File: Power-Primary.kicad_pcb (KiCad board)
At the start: 2 copper layers, 226.1 x 72.4 mm, 77 parts, among them J1 HV in, J10 SPARE, J11 SPARE, J12 SPARE, J13 SPARE, J14 SPARE, J15 SPARE, J16 SPARE, J17 SPARE, J2 Dashboard, J3 Telemetry, J4 Motor, J5 MPPT 1, J6 MPPT 2, J7 BPS, J8 Primary Disconn., J9 SPARE, U1 Mean_Well_12V

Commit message: completed Hannah's edits
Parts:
- removed the G*** at (226.1, 104.1)
- added REF**: MountingHole_3mm, MountingHole:MountingHole_3.7mm, F.Cu at (175.3, 113.0)
- moved REF** 1.60 mm to (237.5, 124.2)
- moved REF** 1.27 mm to (237.5, 60.2)
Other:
- board size 226.1 x 72.4 mm -> 225.8 x 71.9 mm

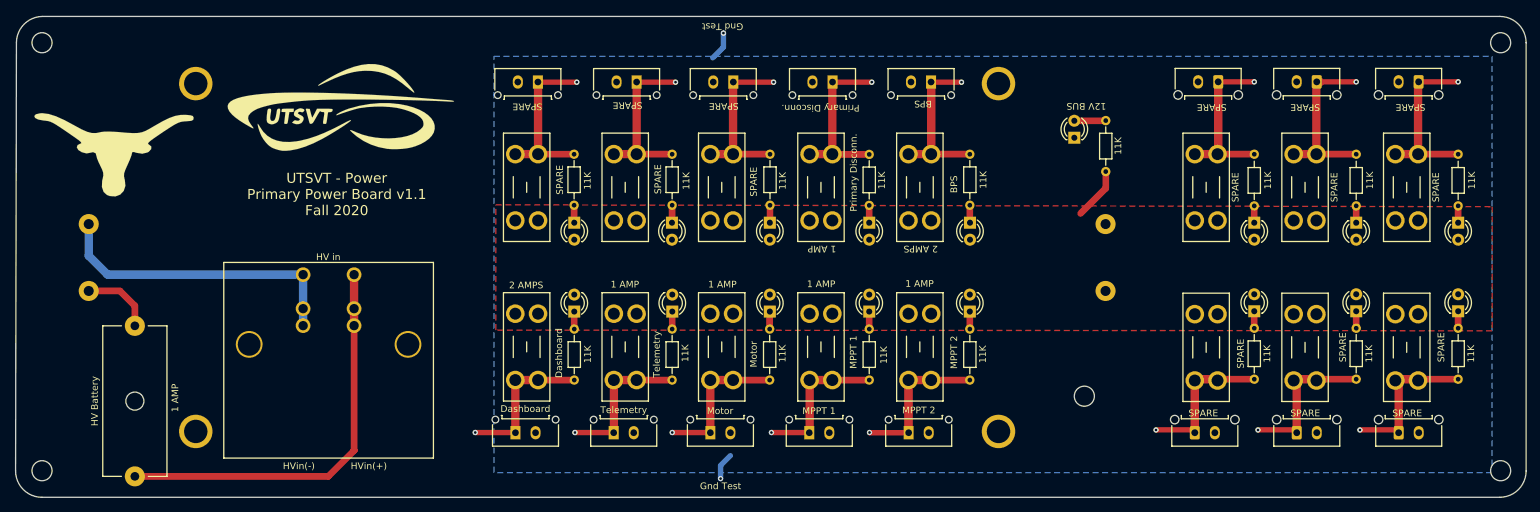
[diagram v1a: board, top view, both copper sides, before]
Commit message: Sijin's edits, mounting hole and power planes
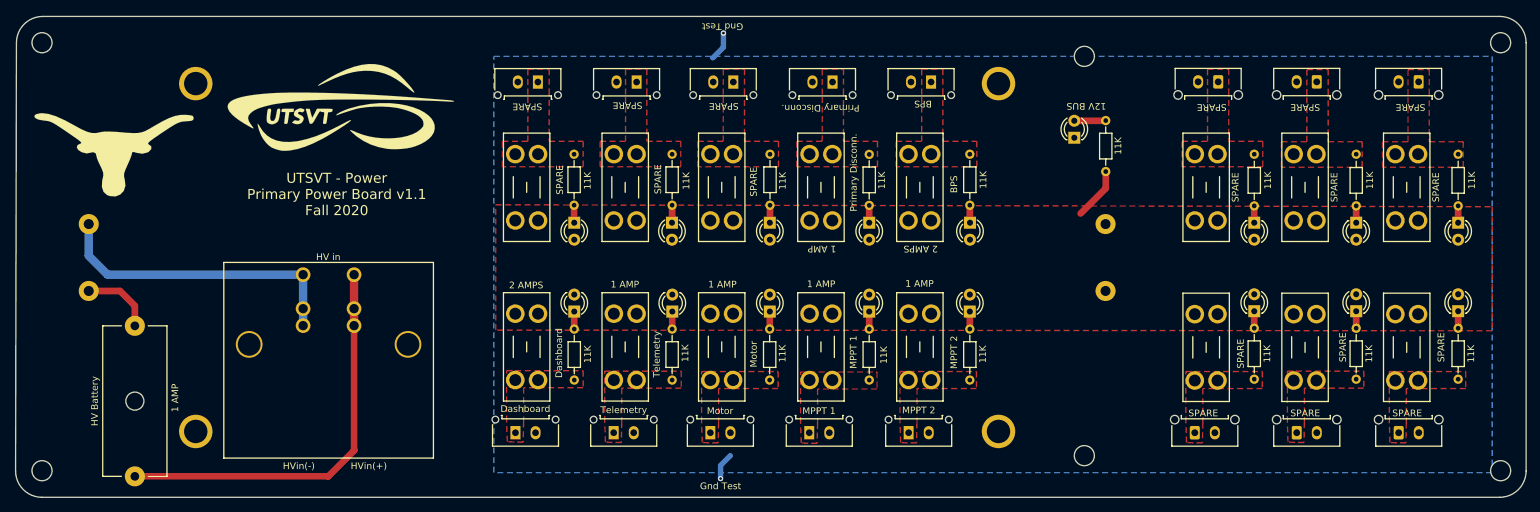
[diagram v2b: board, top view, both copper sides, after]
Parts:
- added REF**: MountingHole_3mm, MountingHole:MountingHole_3.7mm, F.Cu at (175.3, 62.2)
- moved REF** 8.89 mm to (175.3, 121.9)
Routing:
- net Net-(F15-Pad2): track 26.3 -> 0.34 mm, vias 1 -> 0
- net Net-(F9-Pad2): track 25.8 -> 0.14 mm, vias 1 -> 0
- net Net-(F16-Pad2): track 25.9 -> 0.23 mm, vias 1 -> 0
- net Net-(F8-Pad2): track 25.7 -> 0.21 mm, vias 1 -> 0
- net Net-(F11-Pad2): track 25.4 -> 0.12 mm, vias 1 -> 0
- net Net-(F10-Pad2): track 25.3 -> 0.07 mm, vias 1 -> 0
- net Net-(F17-Pad2): track 25.3 -> 0.30 mm, vias 1 -> 0
- net Net-(F7-Pad2): track 24.6 -> 0.12 mm, vias 1 -> 0
- net Net-(F6-Pad2): track 23.0 -> 0.12 mm, vias 1 -> 0
- net Net-(F2-Pad2): track 22.7 -> 0.08 mm, vias 1 -> 0
- net Net-(F4-Pad2): track 22.5 -> 0.04 mm, vias 1 -> 0
- net Net-(F5-Pad2): track 22.7 -> 0.30 mm, vias 1 -> 0
- net Net-(F3-Pad2): track 22.4 -> 0.12 mm, vias 1 -> 0
- net Net-(F13-Pad2): track 22.3 -> 0.00 mm, vias 1 -> 0
- net Net-(F14-Pad2): track 22.3 -> 0.00 mm, vias 1 -> 0
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- added copper zone on F.Cu, net Net-(F10-Pad2)
- added copper zone on F.Cu, net Net-(F11-Pad2)
- added copper zone on F.Cu, net Net-(F12-Pad2)
- added copper zone on F.Cu, net Net-(F13-Pad2)
- added copper zone on F.Cu, net Net-(F14-Pad2)
- added copper zone on F.Cu, net Net-(F15-Pad2)
- added copper zone on F.Cu, net Net-(F16-Pad2)
- added copper zone on F.Cu, net Net-(F17-Pad2)
- added copper zone on F.Cu, net Net-(F2-Pad2)
- added copper zone on F.Cu, net Net-(F3-Pad2)
- added copper zone on F.Cu, net Net-(F4-Pad2)
- added copper zone on F.Cu, net Net-(F5-Pad2)
- added copper zone on F.Cu, net Net-(F6-Pad2)
- added copper zone on F.Cu, net Net-(F7-Pad2)
- added copper zone on F.Cu, net Net-(F8-Pad2)
- added copper zone on F.Cu, net Net-(F9-Pad2)

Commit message: Deletes gerbers from this because added to release and adds dimensions
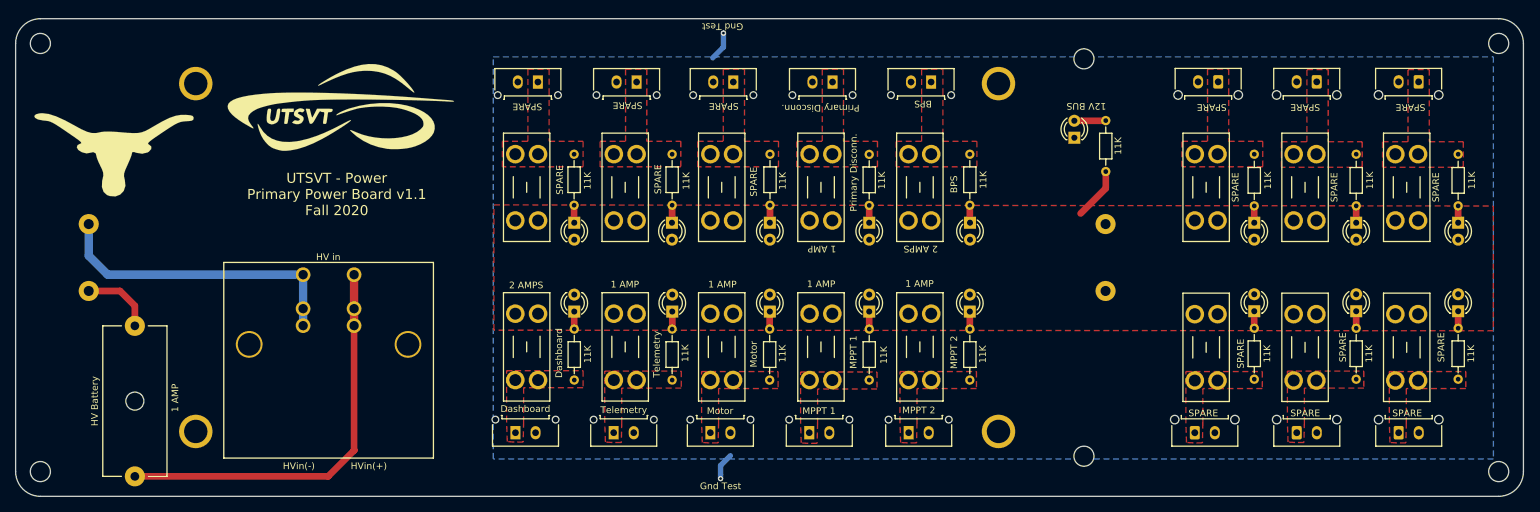
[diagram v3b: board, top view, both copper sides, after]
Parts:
- removed the REF** at (175.3, 121.9)
- removed the REF** at (237.5, 60.2)
- added REF**: MountingHole_3mm, MountingHole:MountingHole_3.7mm, F.Cu at (175.2, 122.0)
- added REF**: MountingHole_3mm, MountingHole:MountingHole_3.7mm, F.Cu at (237.2, 60.3)
- moved REF** 0.37 mm to (175.2, 62.6)
- moved REF** 0.32 mm to (237.2, 124.3)
- moved REF** 0.28 mm to (19.2, 124.3)
- moved REF** 0.27 mm to (19.2, 60.3)
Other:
- board size 225.8 x 71.9 mm -> 225.4 x 71.4 mm
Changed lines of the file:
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@@
-(kicad_pcb (version 20171130) (host pcbnew "(5.1.6)-1")
+(kicad_pcb (version 20171130) (host pcbnew "(5.1.5)-3")
   (general
     (thickness 1.6)
-    (drawings 27)
+    (drawings 29)
     (tracks 95)
     (zones 0)
@@
     (44 Edge.Cuts user)
     (45 Margin user)
-    (46 B.CrtYd user)
-    (47 F.CrtYd user)
-    (48 B.Fab user)
-    (49 F.Fab user)
+    (46 B.CrtYd user hide)
+    (47 F.CrtYd user hide)
+    (48 B.Fab user hide)
+    (49 F.Fab user hide)
   )
   (setup
-    (last_trace_width 0.25)
+    (last_trace_width 0.8)
     (user_trace_width 0.8)
     (user_trace_width 1)
@@
       (drillshape 0)
       (scaleselection 1)
-      (outputdirectory ""))
+      (outputdirectory "Gerbers/"))
   )
   (net 0 "")
@@
   )
   (module MountingHole:MountingHole_3.7mm (layer F.Cu)
-    (at 175.26 62.23)
+    (at 175.2 62.6)
     (descr "Mounting Hole 3.7mm, no annular")
     (tags "mounting hole 3.7mm no annular")
@@
   )
   (module MountingHole:MountingHole_3.7mm (layer F.Cu)
-    (at 175.26 121.92)
+    (at 175.2 122)
     (descr "Mounting Hole 3.7mm, no annular")
     (tags "mounting hole 3.7mm no annular")
@@
   )
   (module MountingHole:MountingHole_3.7mm (layer F.Cu)
-    (at 19.44624 60.19292)
+    (at 19.2 60.3)
     (descr "Mounting Hole 3.7mm, no annular")
     (tags "mounting hole 3.7mm no annular")
@@
   )
   (module MountingHole:MountingHole_3.7mm (layer F.Cu)
-    (at 237.49 60.19292)
+    (at 237.2 60.3)
     (descr "Mounting Hole 3.7mm, no annular")
     (tags "mounting hole 3.7mm no annular")
@@
   )
   (module MountingHole:MountingHole_3.7mm (layer F.Cu)
-    (at 237.49 124.17044)
+    (at 237.2 124.3)
     (descr "Mounting Hole 3.7mm, no annular")
     (tags "mounting hole 3.7mm no annular")
@@
   )
   (module MountingHole:MountingHole_3.7mm (layer F.Cu)
-    (at 19.44624 124.17044)
+    (at 19.2 124.3)
     (descr "Mounting Hole 3.7mm, no annular")
     (tags "mounting hole 3.7mm no annular")
@@
     )
   )
-  (gr_arc (start 237.363 124.206) (end 237.363 128.143) (angle -90) (layer Edge.Cuts) (width 0.15))
-  (gr_arc (start 19.558 60.198) (end 19.558 56.261) (angle -90) (layer Edge.Cuts) (width 0.15))
-  (gr_arc (start 19.431 124.206) (end 15.494 124.206) (angle -90) (layer Edge.Cuts) (width 0.15))
-  (gr_arc (start 237.363 60.198) (end 241.3 60.198) (angle -90) (layer Edge.Cuts) (width 0.15))
+  (dimension 225.4 (width 0.15) (layer Cmts.User)
+    (gr_text "225.400 mm" (at 128.2 52.2) (layer Cmts.User)
+      (effects (font (size 1 1) (thickness 0.15)))
+    )
+    (feature1 (pts (xy 15.5 60.3) (xy 15.5 52.913579)))
+    (feature2 (pts (xy 240.9 60.3) (xy 240.9 52.913579)))
+    (crossbar (pts (xy 240.9 53.5) (xy 15.5 53.5)))
+    (arrow1a (pts (xy 15.5 53.5) (xy 16.626504 52.913579)))
+    (arrow1b (pts (xy 15.5 53.5) (xy 16.626504 54.086421)))
+    (arrow2a (pts (xy 240.9 53.5) (xy 239.773496 52.913579)))
+    (arrow2b (pts (xy 240.9 53.5) (xy 239.773496 54.086421)))
+  )
+  (dimension 71.4 (width 0.15) (layer Cmts.User)
+    (gr_text "71.400 mm" (at 246.6 92.3 270) (layer Cmts.User)
+      (effects (font (size 1 1) (thickness 0.15)))
+    )
+    (feature1 (pts (xy 237.2 128) (xy 245.886421 128)))
+    (feature2 (pts (xy 237.2 56.6) (xy 245.886421 56.6)))
+    (crossbar (pts (xy 245.3 56.6) (xy 245.3 128)))
+    (arrow1a (pts (xy 245.3 128) (xy 244.713579 126.873496)))
+    (arrow1b (pts (xy 245.3 128) (xy 245.886421 126.873496)))
+    (arrow2a (pts (xy 245.3 56.6) (xy 244.713579 57.726504)))
+    (arrow2b (pts (xy 245.3 56.6) (xy 245.886421 57.726504)))
+  )
+  (gr_line (start 237.2 128) (end 19.2 128) (layer Edge.Cuts) (width 0.15))
+  (gr_line (start 240.9 60.3) (end 240.9 124.3) (layer Edge.Cuts) (width 0.15))
+  (gr_line (start 19.2 56.6) (end 237.2 56.6) (layer Edge.Cuts) (width 0.15))
+  (gr_line (start 15.5 60.3) (end 15.5 124.3) (layer Edge.Cuts) (width 0.15))
+  (gr_arc (start 19.2 124.3) (end 15.5 124.3) (angle -90) (layer Edge.Cuts) (width 0.15))
+  (gr_arc (start 237.2 124.3) (end 237.2 128) (angle -90) (layer Edge.Cuts) (width 0.15))
+  (gr_arc (start 237.2 60.3) (end 240.9 60.3) (angle -90) (layer Edge.Cuts) (width 0.15))
+  (gr_arc (start 19.2 60.3) (end 19.2 56.6) (angle -90) (layer Edge.Cuts) (width 0.15))
   (gr_text "1 AMP" (at 136.0424 91.0082 180) (layer F.SilkS)
     (effects (font (size 1 1) (thickness 0.15)))
@@
     (effects (font (size 1.5 1.5) (thickness 0.375)))
   )
-  (gr_line (start 241.3 60.198) (end 241.3 124.206) (layer Edge.Cuts) (width 0.15))
   (gr_text "Vout(-)" (at 171.196 97.1042) (layer B.SilkS)
     (effects (font (size 1.5 1.5) (thickness 0.3)) (justify mirror))
@@
     (effects (font (size 1.5 1.5) (thickness 0.3)) (justify mirror))
   )
-  (gr_line (start 15.494 124.206) (end 15.621 60.198) (layer Edge.Cuts) (width 0.15))
-  (gr_line (start 237.363 128.143) (end 19.431 128.143) (layer Edge.Cuts) (width 0.15))
-  (gr_line (start 19.558 56.261) (end 237.363 56.261) (layer Edge.Cuts) (width 0.15))
   (via (at 121.3104 58.7502) (size 0.8) (drill 0.4) (layers F.Cu B.Cu) (net 1))
   (via (at 120.8786 125.349) (size 0.8) (drill 0.4) (layers F.Cu B.Cu) (net 1))
@@
     (polygon
       (pts
-        (xy 86.995 62.23) (xy 236.22 62.23) (xy 236.22 124.46) (xy 86.995 124.46)
+        (xy 86.9 62.3) (xy 236.4 62.3) (xy 236.4125 122.4) (xy 86.9 122.4)
       )
     )
@@
     (polygon
       (pts
-        (xy 87.2744 84.42452) (xy 236.22508 84.70646) (xy 236.21492 103.25354) (xy 87.2744 103.1494)
+        (xy 87 84.43756) (xy 236.4 84.6) (xy 236.39492 103.25354) (xy 87 103.16244)
       )
     )
